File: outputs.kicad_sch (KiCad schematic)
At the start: 36 parts, among them U16 74HCT574, U17 74HCT574, U18 74HCT574, U19 74HCT574, U20 74HCT574, U21 74HCT574, U22 74HCT574, U23 74HCT574, U24 74HCT574, U25 74HCT574, U26 74HCT574, U27 74HCT574

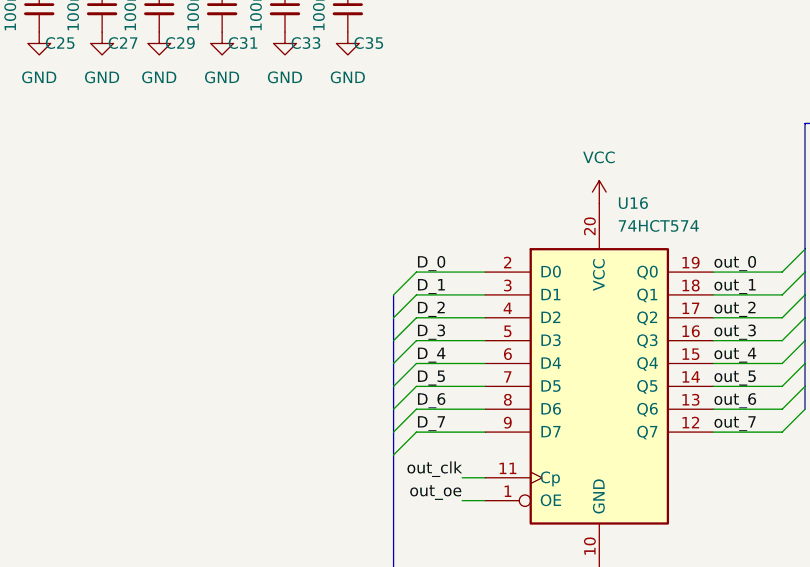
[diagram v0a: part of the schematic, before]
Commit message: Turns out 324As don't really exist anymore
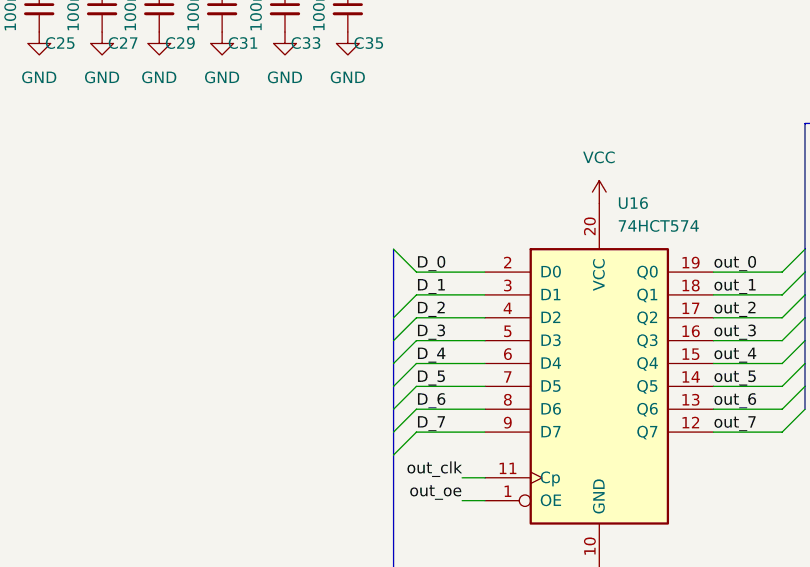
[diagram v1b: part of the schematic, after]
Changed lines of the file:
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@@
     (stroke (width 0) (type default) (color 0 0 0 0))
   )
-  (bus_entry (at -29.21 68.58) (size 2.54 -2.54)
+  (bus_entry (at -26.67 66.04) (size -2.54 -2.54)
     (stroke (width 0) (type default) (color 0 0 0 0))
   )
@@
     (stroke (width 0) (type default) (color 0 0 0 0))
   )
-  (bus (pts (xy -29.21 68.58) (xy -29.21 71.12))
+  (bus (pts (xy -29.21 63.5) (xy -29.21 71.12))
     (stroke (width 0) (type default) (color 0 0 0 0))
   )
